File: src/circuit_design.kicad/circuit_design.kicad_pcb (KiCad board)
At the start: 2 copper layers, 205.7 x 170.8 mm, 183 parts, among them J1 CONN_BAT, Q1 BT134-600E, Q2 BT134-600E, Q3 BT134-600E, Q4 BT134-600E, U1 К176ИЕ12, U10 К155ЛА4, U11 К155ЛИ1, U12 К155ЛА1, U13 К155ИЕ5, U14 К155ЛЛ1, U15 К155ЛН1, U16 К155ЛИ1, U17 К155ТВ15, U18 К155ИЕ5, U19 К155ЛП5, U2 К155ЛП10, U20 К155ИВ1, U21 К155ИД7, U22 К155ИД4, U23 К155ЛН1, U24 К155ЛП10, U25 MOC3062M, U26 MOC3062M, U27 MOC3062M, U28 MOC3062M, U29 LM7806_TO220, U3 К155ЛЕ3, U30 SC6038, U31 К155ЛЕ1, U32 К155ЛН1, U33 К155ЛИ1, U34 К155ЛА4, U35 К155ТВ15, U36 К155ТЛ2, U37 4020, U38 LM7806_TO220, U39 К155ЛН1, U4 К155ЛН1, U5 К155ЛИ1, U6 К155ЛЛ1, U7 4020, U8 ICL7660, U9 К155ИЕ5, Y1 32768

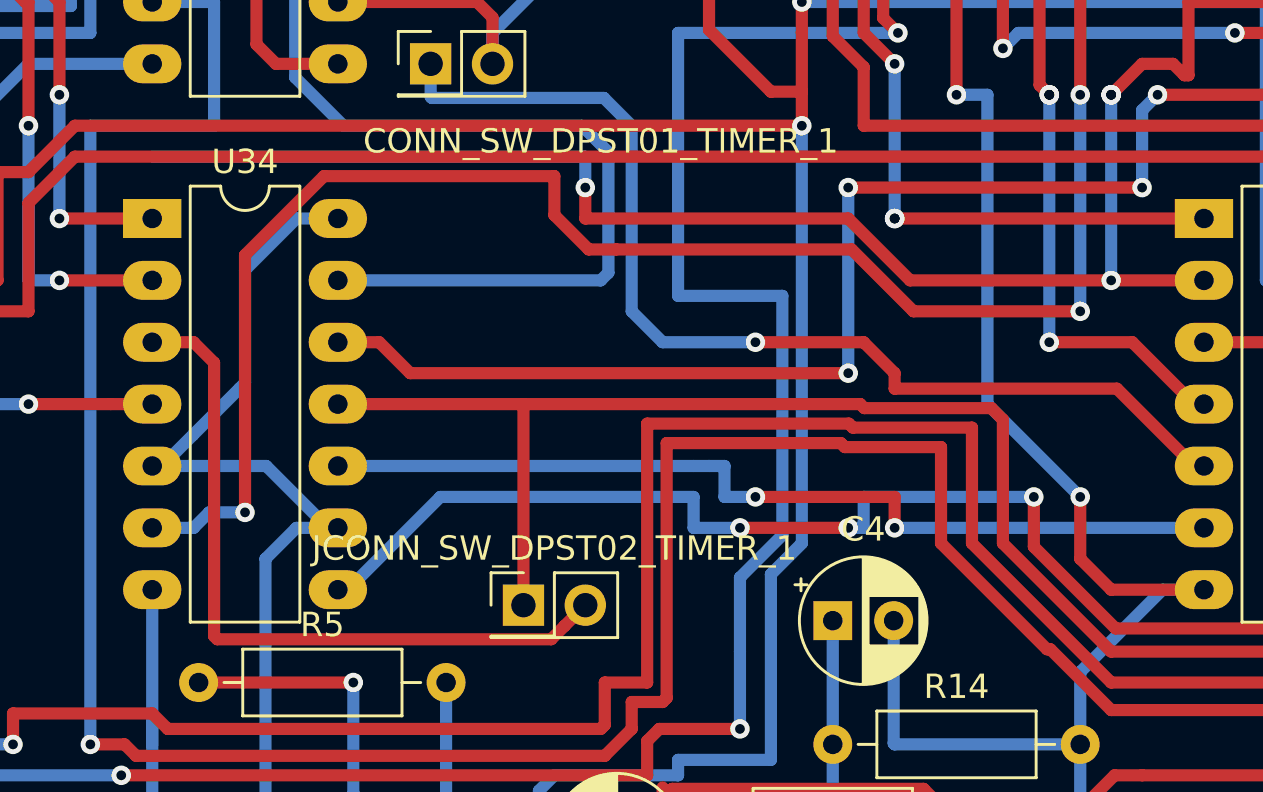
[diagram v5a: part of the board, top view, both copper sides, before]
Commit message: The 24-hours timer JCONN_SW_DPST02_TIMER_1 connector placement was changed (to be much more far from the other inputs).
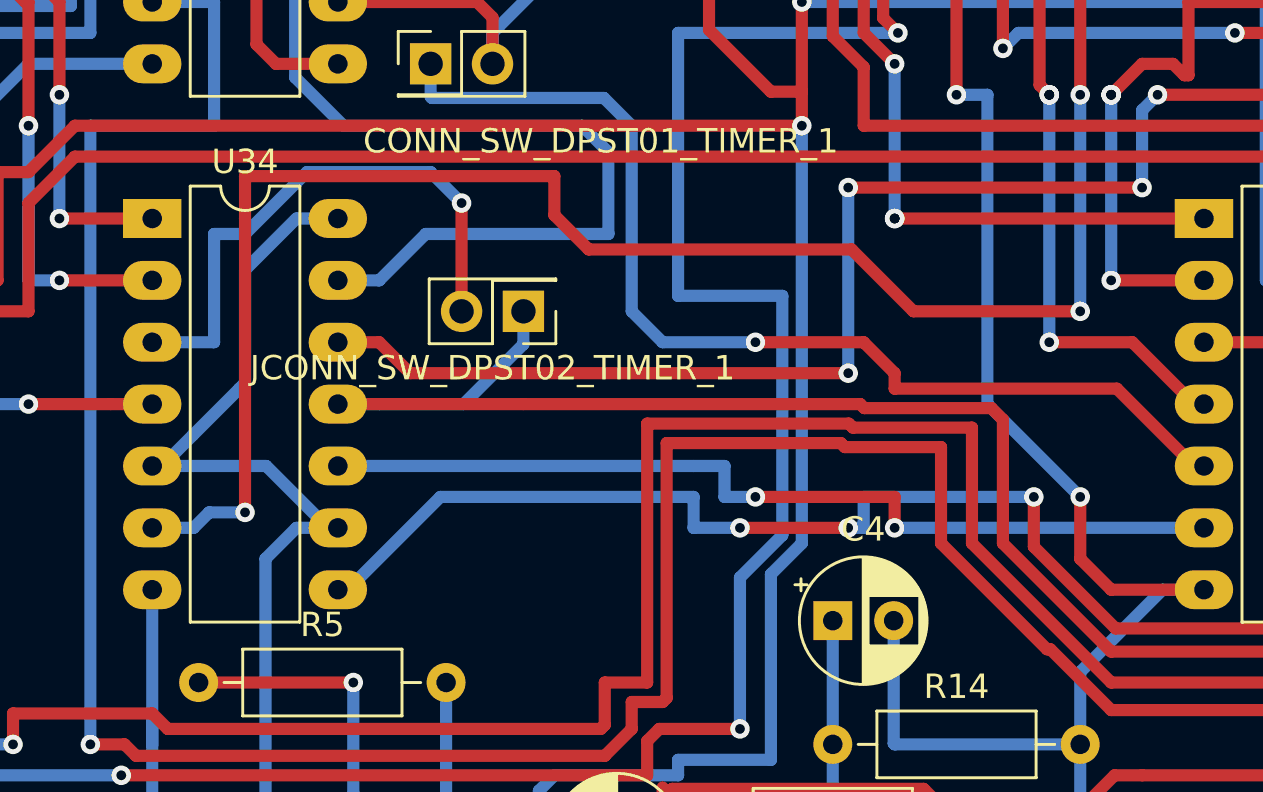
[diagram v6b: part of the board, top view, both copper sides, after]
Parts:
- moved JCONN_SW_DPST02_TIMER_1 12.1 mm to (83.8, 91.4), turned to 180 degrees
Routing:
- net Net-(U32-Pad2): track 89.9 -> 46.9 mm, vias 4 -> 3
- net Net-(JCONN_SW_DPST02_TIMER_1-Pad2): track 30.0 -> 23.2 mm, vias 0 -> 1
- net Net-(U33-Pad4): track 81.4 -> 83.3 mm
- net Net-(JCONN_SW_DPST02_TIMER_1-Pad1): track 176.5 -> 178.2 mm
- net Net-(U34-Pad13): track 97.9 -> 97.0 mm
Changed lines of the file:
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@@
     (thickness 1.6)
     (drawings 19)
-    (tracks 3808)
+    (tracks 3806)
     (zones 0)
     (modules 183)
@@
   )
   (module Connector_PinHeader_2.54mm:PinHeader_2x01_P2.54mm_Vertical (layer F.Cu)
-    (at 83.82 103.505)
+    (at 83.82 91.44 180)
     (descr "Through hole straight pin header, 2x01, 2.54mm pitch, double rows")
     (tags "Through hole pin header THT 2x01 2.54mm double row")
-    (fp_text reference JCONN_SW_DPST02_TIMER_1 (at 1.27 -2.33) (layer F.SilkS)
+    (fp_text reference JCONN_SW_DPST02_TIMER_1 (at 1.27 -2.33 180) (layer F.SilkS)
       (effects (font (size 1 1) (thickness 0.15)))
     )
-    (fp_text value Conn_01x02_Male (at 1.27 2.33) (layer F.Fab)
+    (fp_text value Conn_01x02_Male (at 1.27 2.33 180) (layer F.Fab)
       (effects (font (size 1 1) (thickness 0.15)))
     )
@@
     (fp_line (start 4.35 1.8) (end 4.35 -1.8) (layer F.CrtYd) (width 0.05))
     (fp_line (start 4.35 -1.8) (end -1.8 -1.8) (layer F.CrtYd) (width 0.05))
-    (fp_text user %R (at 1.27 0 90) (layer F.Fab)
+    (fp_text user %R (at 1.27 0 270) (layer F.Fab)
       (effects (font (size 1 1) (thickness 0.15)))
     )
-    (pad 1 thru_hole rect (at 0 0) (size 1.7 1.7) (drill 1) (layers *.Cu *.Mask)
+    (pad 1 thru_hole rect (at 0 0 180) (size 1.7 1.7) (drill 1) (layers *.Cu *.Mask)
       (net 167 "Net-(JCONN_SW_DPST02_TIMER_1-Pad1)"))
-    (pad 2 thru_hole oval (at 2.54 0) (size 1.7 1.7) (drill 1) (layers *.Cu *.Mask)
+    (pad 2 thru_hole oval (at 2.54 0 180) (size 1.7 1.7) (drill 1) (layers *.Cu *.Mask)
       (net 168 "Net-(JCONN_SW_DPST02_TIMER_1-Pad2)"))
     (model ${KISYS3DMOD}/Connector_PinHeader_2.54mm.3dshapes/PinHeader_2x01_P2.54mm_Vertical.wrl
@@
   (segment (start 111.125 78.74) (end 111.125 81.74999) (width 0.5) (layer F.Cu) (net 91))
   (segment (start 111.125 81.74999) (end 110.95999 81.74999) (width 0.5) (layer F.Cu) (net 91))
-  (segment (start 99.695 90.17) (end 107.95 90.17) (width 0.5) (layer F.Cu) (net 91))
-  (segment (start 97.155 87.63) (end 99.695 90.17) (width 0.5) (layer F.Cu) (net 91))
-  (segment (start 86.36 87.63) (end 97.155 87.63) (width 0.5) (layer F.Cu) (net 91))
-  (segment (start 86.36 86.36) (end 86.36 87.63) (width 0.5) (layer F.Cu) (net 91))
-  (via blind (at 86.36 86.36) (size 0.8) (drill 0.4) (layers F.Cu B.Cu) (net 91))
-  (segment (start 86.36 85.09) (end 86.36 86.36) (width 0.5) (layer B.Cu) (net 91))
-  (segment (start 68.58 85.09) (end 86.36 85.09) (width 0.5) (layer B.Cu) (net 91))
   (segment (start 115.57 73.66) (end 114.3 73.66) (width 0.5) (layer F.Cu) (net 91))
   (via blind (at 107.95 82.55) (size 0.8) (drill 0.4) (layers F.Cu B.Cu) (net 91))
@@
   (segment (start 71.439999 61.416001) (end 74.44999 64.425992) (width 0.5) (layer B.Cu) (net 157))
   (segment (start 76.2 55.743998) (end 71.439999 60.503999) (width 0.5) (layer B.Cu) (net 157))
-  (segment (start 87.310001 84.908617) (end 87.310001 89.854999) (width 0.5) (layer B.Cu) (net 157))
   (segment (start 76.430798 83.82) (end 86.221384 83.82) (width 0.5) (layer B.Cu) (net 157))
   (segment (start 86.221384 83.82) (end 87.310001 84.908617) (width 0.5) (layer B.Cu) (net 157))
-  (segment (start 86.995 90.17) (end 76.2 90.17) (width 0.5) (layer B.Cu) (net 157) (status 20))
-  (segment (start 87.310001 89.854999) (end 86.995 90.17) (width 0.5) (layer B.Cu) (net 157))
   (segment (start 76.2 38.1) (end 76.2 55.743998) (width 0.5) (layer B.Cu) (net 157))
   (segment (start 79.298616 28.016384) (end 78.74 28.575) (width 0.5) (layer B.Cu) (net 157))
   (segment (start 76.2 34.925) (end 76.366364 34.758636) (width 0.5) (layer B.Cu) (net 157))
+  (segment (start 77.9 90.17) (end 79.805 88.265) (width 0.5) (layer B.Cu) (net 157))
+  (segment (start 76.2 90.17) (end 77.9 90.17) (width 0.5) (layer B.Cu) (net 157))
+  (segment (start 79.805 88.265) (end 87.310001 88.265) (width 0.5) (layer B.Cu) (net 157))
+  (segment (start 87.310001 84.908617) (end 87.310001 88.265) (width 0.5) (layer B.Cu) (net 157))
   (segment (start 81.915 23.895) (end 80.01 25.8) (width 0.5) (layer B.Cu) (net 158) (status 10))
   (segment (start 81.915 23.495) (end 81.915 23.895) (width 0.5) (layer B.Cu) (net 158) (status 30))
@@
   (segment (start 205.105 54.794998) (end 205.105 48.895) (width 0.5) (layer F.Cu) (net 166))
   (segment (start 76.2 95.25) (end 83.82 95.25) (width 0.5) (layer F.Cu) (net 167) (status 10))
-  (segment (start 83.82 95.25) (end 83.82 103.505) (width 0.5) (layer F.Cu) (net 167) (status 20))
   (via blind (at 116.84 105.41) (size 0.8) (drill 0.4) (layers F.Cu B.Cu) (net 167))
   (via blind (at 123.19 100.965) (size 0.8) (drill 0.4) (layers F.Cu B.Cu) (net 167))
@@
   (segment (start 103.505 95.885) (end 103.03501 95.41501) (width 0.5) (layer F.Cu) (net 167))
   (segment (start 97.816394 95.41501) (end 97.651384 95.25) (width 0.5) (layer F.Cu) (net 167))
-  (segment (start 68.58 92.71) (end 70.28 92.71) (width 0.5) (layer F.Cu) (net 168) (status 10))
-  (segment (start 70.28 92.71) (end 71.12 93.55) (width 0.5) (layer F.Cu) (net 168))
-  (segment (start 71.12 93.55) (end 71.12 104.775) (width 0.5) (layer F.Cu) (net 168))
-  (segment (start 85.510001 104.354999) (end 86.36 103.505) (width 0.5) (layer F.Cu) (net 168) (status 30))
-  (segment (start 84.959999 104.905001) (end 85.510001 104.354999) (width 0.5) (layer F.Cu) (net 168) (status 20))
-  (segment (start 71.250001 104.905001) (end 84.959999 104.905001) (width 0.5) (layer F.Cu) (net 168))
-  (segment (start 71.12 104.775) (end 71.250001 104.905001) (width 0.5) (layer F.Cu) (net 168))
+  (segment (start 77.9 95.25) (end 76.2 95.25) (width 0.5) (layer B.Cu) (net 167))
+  (segment (start 81.36 95.25) (end 77.9 95.25) (width 0.5) (layer B.Cu) (net 167))
+  (segment (start 83.82 92.79) (end 81.36 95.25) (width 0.5) (layer B.Cu) (net 167))
+  (segment (start 83.82 91.44) (end 83.82 92.79) (width 0.5) (layer B.Cu) (net 167))
+  (segment (start 81.28 86.995) (end 81.28 86.995) (width 0.5) (layer B.Cu) (net 168))
+  (via blind (at 81.28 86.995) (size 0.8) (drill 0.4) (layers F.Cu B.Cu) (net 168))
+  (segment (start 81.28 86.995) (end 81.28 91.44) (width 0.5) (layer F.Cu) (net 168))
+  (segment (start 80.01 85.725) (end 81.28 86.995) (width 0.5) (layer B.Cu) (net 168))
+  (segment (start 72.39 88.265) (end 74.93 85.725) (width 0.5) (layer B.Cu) (net 168))
+  (segment (start 71.12 88.265) (end 71.12 92.71) (width 0.5) (layer B.Cu) (net 168))
+  (segment (start 71.12 88.265) (end 72.39 88.265) (width 0.5) (layer B.Cu) (net 168))
+  (segment (start 71.12 92.71) (end 68.58 92.71) (width 0.5) (layer B.Cu) (net 168))
+  (segment (start 74.93 85.725) (end 80.01 85.725) (width 0.5) (layer B.Cu) (net 168))
   (segment (start 111.76 100.33) (end 99.06 100.33) (width 0.5) (layer B.Cu) (net 169) (status 10))
   (segment (start 76.2 97.79) (end 90.805 97.79) (width 0.5) (layer B.Cu) (net 169) (status 10))
@@
   (segment (start 70.915 99.695) (end 72.39 99.695) (width 0.5) (layer B.Cu) (net 170))
   (via blind (at 72.39 99.695) (size 0.8) (drill 0.4) (layers F.Cu B.Cu) (net 170))
-  (segment (start 72.39 89.130798) (end 75.630788 85.89001) (width 0.5) (layer F.Cu) (net 170))
-  (segment (start 72.39 99.695) (end 72.39 89.130798) (width 0.5) (layer F.Cu) (net 170))
-  (segment (start 75.630788 85.89001) (end 85.09 85.89001) (width 0.5) (layer F.Cu) (net 170))
-  (segment (start 85.09 87.491384) (end 86.498616 88.9) (width 0.5) (layer F.Cu) (net 170))
-  (segment (start 85.09 85.89001) (end 85.09 87.491384) (width 0.5) (layer F.Cu) (net 170))
-  (segment (start 86.498616 88.9) (end 87.63 88.9) (width 0.5) (layer F.Cu) (net 170))
-  (segment (start 97.293616 88.9) (end 99.833616 91.44) (width 0.5) (layer F.Cu) (net 170))
-  (segment (start 99.833616 91.44) (end 106.68 91.44) (width 0.5) (layer F.Cu) (net 170))
   (via blind (at 106.68 91.44) (size 0.8) (drill 0.4) (layers F.Cu B.Cu) (net 170))
   (segment (start 106.68 91.44) (end 106.68 82.55) (width 0.5) (layer B.Cu) (net 170))
@@
   (segment (start 106.68 82.55) (end 106.68 68.58) (width 0.5) (layer F.Cu) (net 170))
   (segment (start 106.68 68.58) (end 111.76 68.58) (width 0.5) (layer F.Cu) (net 170) (status 20))
-  (segment (start 87.63 88.9) (end 97.293616 88.9) (width 0.5) (layer F.Cu) (net 170))
+  (segment (start 72.39 87.63) (end 72.39 99.695) (width 0.5) (layer F.Cu) (net 170))
+  (segment (start 72.39 85.89001) (end 72.39 87.63) (width 0.5) (layer F.Cu) (net 170))
+  (segment (start 97.293616 88.9) (end 86.498616 88.9) (width 0.5) (layer F.Cu) (net 170))
+  (segment (start 106.68 91.44) (end 99.833616 91.44) (width 0.5) (layer F.Cu) (net 170))
+  (segment (start 85.09 85.89001) (end 72.39 85.89001) (width 0.5) (layer F.Cu) (net 170))
+  (segment (start 86.498616 88.9) (end 85.09 87.491384) (width 0.5) (layer F.Cu) (net 170))
+  (segment (start 99.833616 91.44) (end 97.293616 88.9) (width 0.5) (layer F.Cu) (net 170))
+  (segment (start 85.09 87.491384) (end 85.09 85.89001) (width 0.5) (layer F.Cu) (net 170))
   (segment (start 119.38 68.58) (end 121.285 68.58) (width 0.5) (layer B.Cu) (net 171) (status 10))
   (segment (start 121.285 70.485) (end 121.92 71.12) (width 0.5) (layer B.Cu) (net 171))
